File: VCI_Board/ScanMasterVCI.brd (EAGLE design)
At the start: 53 x 39.4 mm, 77 parts, among them IC1 XMEGA16A4A, Q13 MMBT3904, Q14 MMBT3904, Q15 MMBT3904, Q2 NDC7002N, Q3 MMBT3904, Q5 NTZD5110N, Q6 MMBT3904, Q7 ZXMP6A17G, Q8 MMBT4403, Q9 NDC7002N, U1 MAX17502FATB+, U2 SN65HVDA195-Q1, U3 MAX17502EATB+, U4 L78L08ABUTR

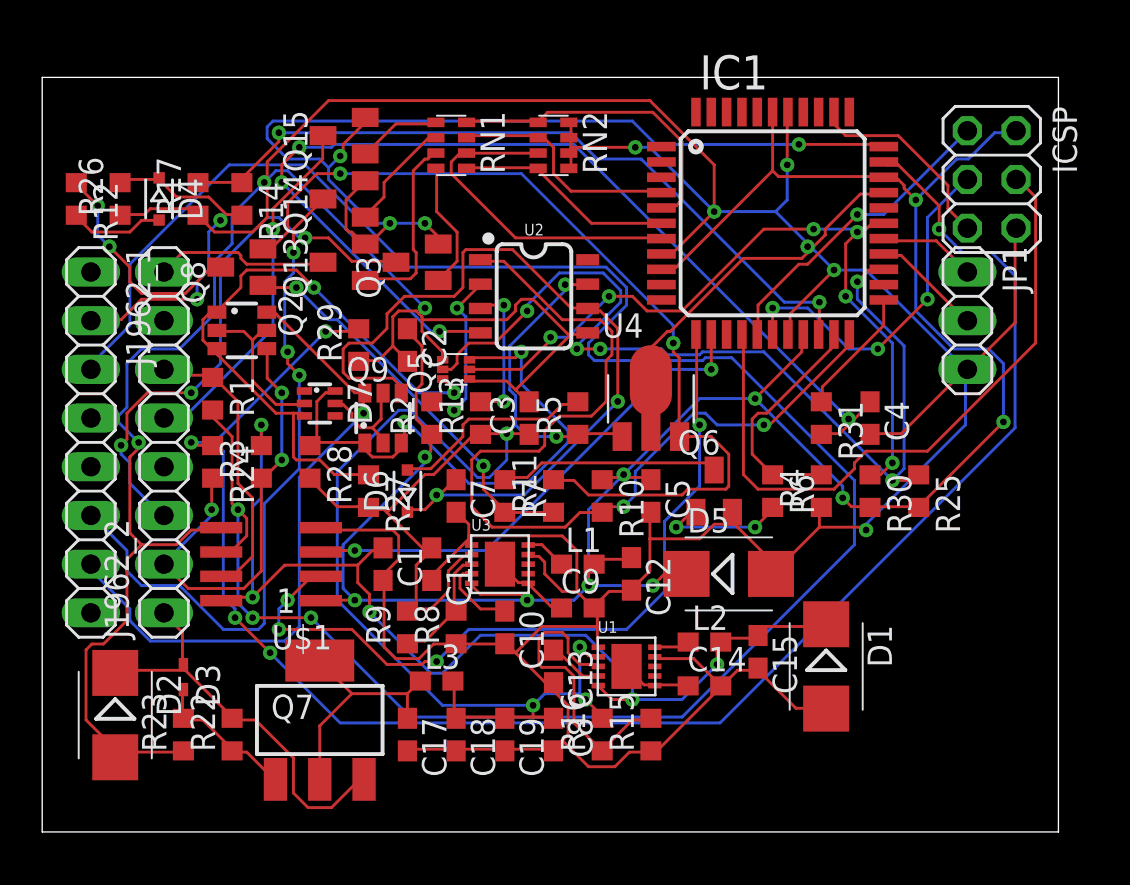
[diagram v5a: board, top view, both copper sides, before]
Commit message: Changed OBD2 connector, refined layout
Decided that it'd be more efficient if I removed all un-used OBD-II pins. Axed about 5 pins and changed the order such that the layout is easier. Managed to get the number of vias down to 68 or so. Separated resistors and capacitors into rows so that I can label them individually.
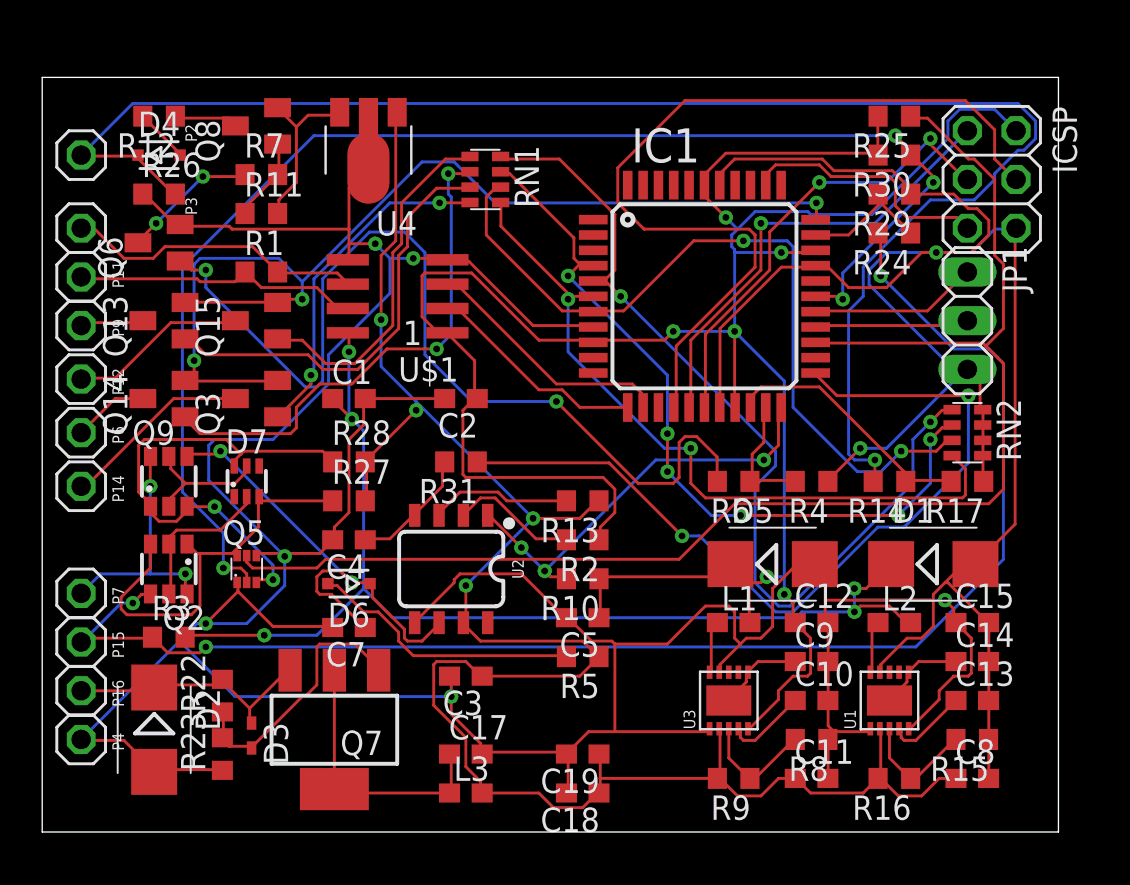
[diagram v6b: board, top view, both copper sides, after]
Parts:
- removed J1962_1, J1962_2: (no value), pinhead:1X08
- added P11, P12, P14, P15, P16, P2, P3, P4, P6, P7, P9: (no value), pinhead:1X01
- moved R17 42.8 mm to (48.3, 20.8), turned to 180 degrees
- moved R24 37.5 mm to (44.5, 33.8), turned to 180 degrees
- moved R14 36.9 mm to (44.2, 20.8), turned to 180 degrees
- moved Q6 31.7 mm to (6.10, 33.3), turned to 90 degrees
- moved R29 29.0 mm to (44.5, 35.8), turned to 180 degrees
- moved C4 27.9 mm to (16.0, 17.8), turned to 180 degrees
- moved RN2 26.3 mm to (48.3, 23.4)
- moved C11 22.7 mm to (40.1, 5.33), turned to 0 degrees
- moved C8 22.0 mm to (48.5, 5.33), turned to 0 degrees
- moved C13 21.9 mm to (48.5, 9.40), turned to 0 degrees
- moved R11 21.2 mm to (11.4, 34.8), turned to 0 degrees
- moved R7 21.0 mm to (11.4, 36.8), turned to 0 degrees
- moved U4 19.6 mm to (17.0, 38.1), turned to 180 degrees
- moved R25 19.6 mm to (44.5, 39.9), turned to 180 degrees
- moved R8 19.4 mm to (40.1, 7.37), turned to 180 degrees
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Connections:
- net GND: now also P4.1; no longer J1962_1.4
- net J1962-11: now also P11.1; no longer J1962_2.6
- net J1962-12: now also P12.1; no longer J1962_2.5
- net J1962-14: now also P14.1; no longer J1962_2.3
- net J1962-15: now also P15.1; no longer J1962_2.2
- net J1962-16: now also P16.1; no longer J1962_2.1
- net J1962-2: now also P2.1; no longer J1962_1.2
- net J1962-3: now also P3.1; no longer J1962_1.3
- net J1962-6: now also P6.1; no longer J1962_1.6
- net J1962-7: now also P7.1; no longer J1962_1.7
- net J1962-9: now also P9.1; no longer J1962_2.8
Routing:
- net J1962-3: track 113.7 -> 15.6 mm, vias 3 -> 0
- net SCI-RX: track 89.3 -> 7.38 mm, vias 5 -> 0
- net J1962-2: track 18.3 -> 82.8 mm, vias 2 -> 1
- net J1962-15: track 24.0 -> 76.0 mm
- net N$10: track 53.9 -> 6.55 mm, vias 4 -> 0
- net N$6: track 6.99 -> 50.1 mm
- net +8V: track 47.5 -> 8.91 mm, vias 2 -> 0
- net ISO-K-TX: track 6.67 -> 44.1 mm, vias 0 -> 2
- net J1962-6: track 36.3 -> 3.95 mm, vias 3 -> 0
- net SCI-B-ENGINE-EN: track 16.5 -> 48.5 mm, vias 0 -> 2
- net SCI-A-TX-EN: track 40.3 -> 71.3 mm, vias 6 -> 4
- net CCD-RX: track 40.6 -> 11.6 mm, vias 4 -> 0
- net SCI-A-ENGINE-EN: track 12.2 -> 40.6 mm, vias 0 -> 6
- net ISO-K-RX: track 49.3 -> 22.4 mm, vias 2 -> 3
- net SCI-A-TRANS-EN: track 11.4 -> 37.9 mm, vias 0 -> 2
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
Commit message: Replaced NDC7002N with NTZD5110N
NDC7002N is out of stock at Digikey, so I am substituting the NTZD5110N. Should be fine, the 5110 just has a lower amp rating than the 7002.
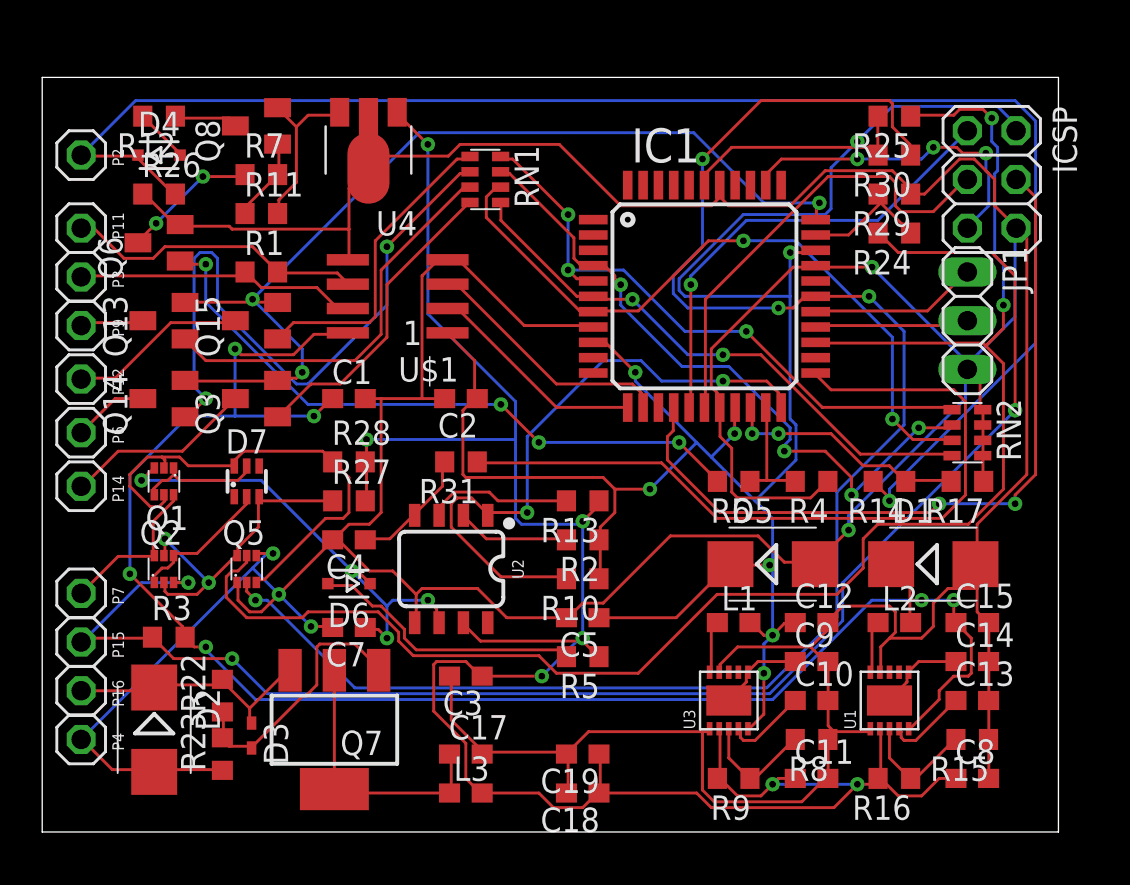
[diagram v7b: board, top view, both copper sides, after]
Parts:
- removed Q9: NDC7002N, customics:SSOT6
- added Q1: NTZD5110N, customics:SOT563
- Q2: value NDC7002N -> NTZD5110N; device customics:SSOT6 -> customics:SOT563
- moved P11 2.54 mm to (2.03, 34.0)
- moved P3 2.54 mm to (2.03, 31.5)
- moved Q2 0.25 mm to (6.35, 16.3), turned to 0 degrees
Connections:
- net ISO-K: now also Q1.3; no longer Q9.4
- net J1962-11: now also R1.2, U$1.6; no longer R1.1, U$1.7
- net J1962-15: now also Q2.3; no longer Q2.4
- net J1962-3: now also R1.1, U$1.7; no longer R1.2, U$1.6
- net J1962-7: now also Q1.6; no longer Q9.6
- net N$1: now also Q2.1, Q2.4; no longer Q2.2, Q2.5
- net N$11: now also Q1.2, Q1.5; no longer Q9.1, Q9.3
- net N$4: now also Q1.1, Q1.4; no longer Q9.2, Q9.5
- net N$5: now also Q2.2, Q2.5; no longer Q2.1, Q2.3
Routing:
- net N$6: track 50.1 -> 34.0 mm, vias 2 -> 4
- net SCI-B-ENGINE-EN: track 48.5 -> 32.4 mm, vias 2 -> 3
- net +5V: track 73.0 -> 88.6 mm
- net SCI-A-TX-EN: track 71.3 -> 86.6 mm
- net +12V: track 101.8 -> 114.4 mm, vias 4 -> 7
- net ISO-K-EN: track 73.5 -> 84.4 mm, vias 0 -> 2
- net ISO-K-RX: track 22.4 -> 33.2 mm, vias 3 -> 2
- net SCI-A-TRANS-EN: track 37.9 -> 29.6 mm
- net N$21: track 26.7 -> 34.4 mm
- net SCI-A-ENGINE-EN: track 40.6 -> 35.1 mm, vias 6 -> 4
- net MOSI: track 45.3 -> 40.2 mm, vias 0 -> 2
- net GND: track 305.0 -> 310.0 mm, vias 7 -> 5
- net J1962-7: track 13.1 -> 8.26 mm, vias 2 -> 0
- net N$5: track 21.7 -> 16.9 mm, vias 0 -> 2
- net SCI-B-TRANS-EN: track 41.0 -> 36.7 mm
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
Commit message: Re-positioned names, removed values
In layout, positioned names so they will be visible during assembly, and deleted values from layout, unneeded. Added another resistor array to save on space, number of vias down to 58.
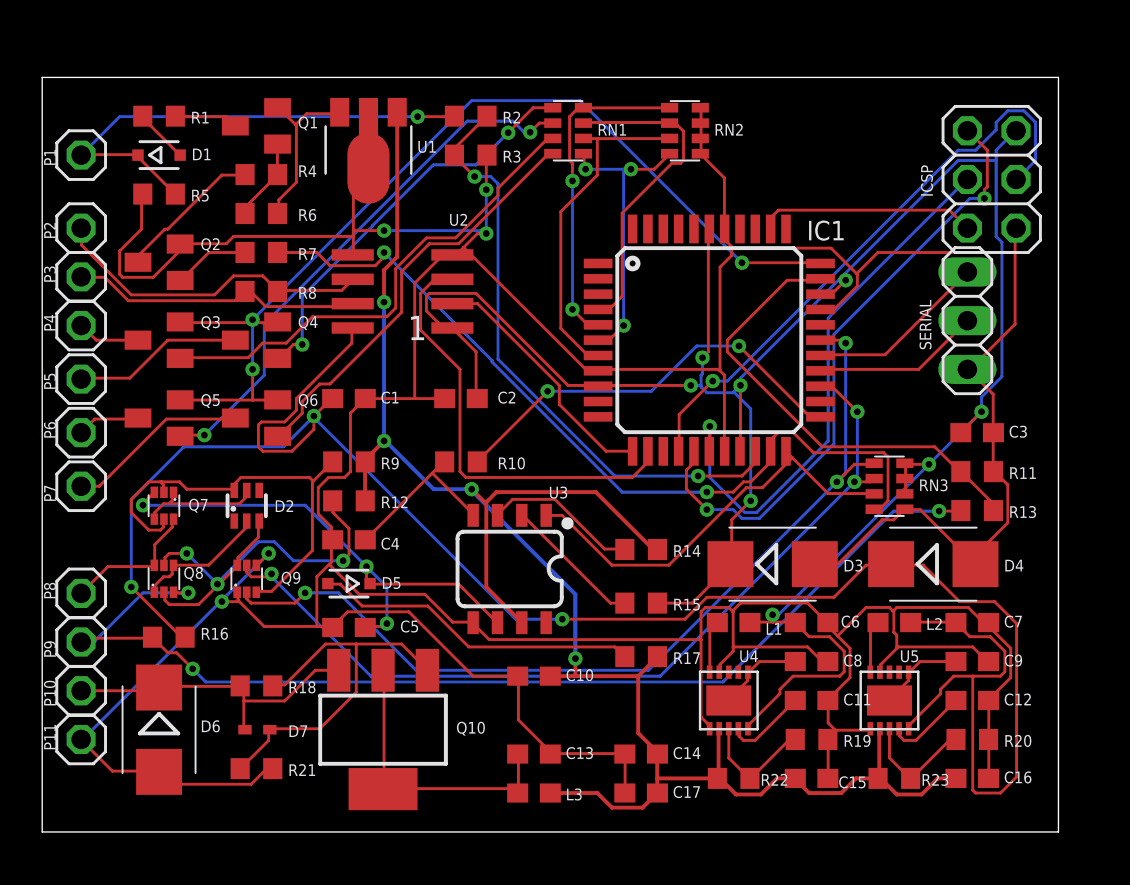
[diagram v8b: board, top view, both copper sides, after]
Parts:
- removed C18: 100uF, adafruit:C0603
- removed C19: 330pF, adafruit:C0603
- removed FRAME1: FRAME-LETTER, SparkFun-Aesthetics:CREATIVE_COMMONS
- removed P14, P15: (no value), pinhead:1X01
- removed Q13, Q14, Q15: MMBT3904, semicon-smd-ipc:SOT23
- removed R24, R31: 1k, adafruit:R0603
- removed R25, R26, R30: 10k, adafruit:R0603
- removed R27, R28: 9.09M, adafruit:R0603
- removed R29: 1910, adafruit:R0603
- removed U$1: ISO1050, customics:SOP08
- added C16: 2.2uF, adafruit:C0603
- added C6: 22uF, adafruit:C0603
- added P1, P8: (no value), pinhead:1X01
- added Q10: ZXMP6A17G, customics:SOT223
- added Q4: MMBT3904, semicon-smd-ipc:SOT23
- added Q9: NTZD5110N, customics:SOT563
- added R18: 200k, adafruit:R0603
- added R19, R20: 866k, adafruit:R0603
- added R21: 20k, adafruit:R0603
- added RN3: 742C083104JP, resistor-net:CTS742C083
- added U5: MAX17502FATB+, customics:TDFN-10
- C10, C13: value 1uF -> 0.1uF
- C11: value 2.2uF -> 1uF
- C12: value 22uF -> 1uF
- C14: value 3300pF -> 330pF
- C15: value 22uF -> 2.2uF
- C17: value 0.1uF -> 100uF
- C5: value 0.1uF -> 220pF
- C7: value 220pF -> 22uF
- C8: value 2.2uF -> 3300pF
- D1: value SMAJ5.0A -> 1N4148WX; device diode:SMB -> diode:SOD323-R
- D2: value 1.5SMC43AT3G -> BZX84C2V4S; device diode:SMB -> customics:SOT363
- D3: value MM5Z10V -> SMLVT3V3; device diode:SOD523 -> diode:SMB
- D4: value 1N4148WX -> SMAJ5.0A; device diode:SOD323-R -> diode:SMB
- D5: value SMLVT3V3 -> 1N4148WX; device diode:SMB -> diode:SOD323-R
- D6: value 1N4148WX -> 1.5SMC43AT3G; device diode:SOD323-R -> diode:SMB
- D7: value BZX84C2V4S -> MM5Z10V; device customics:SOT363 -> diode:SOD523
- Q1: value NTZD5110N -> MMBT4403; device customics:SOT563 -> transistor-pnp:SOT23-BEC
- Q2, Q5: value NTZD5110N -> MMBT3904; device customics:SOT563 -> semicon-smd-ipc:SOT23
- Q7: value ZXMP6A17G -> NTZD5110N; device customics:SOT223 -> customics:SOT563
- Q8: value MMBT4403 -> NTZD5110N; device transistor-pnp:SOT23-BEC -> customics:SOT563
- R1: value 120 -> 47
- R10: value 100K -> 1k
- R11: value 1k -> 1910
- R12: value 47 -> 9.09M
- R13: value 10k -> 1k
- R14: value 7.5k -> 10k
- R15: value 866k -> 100k
- R16: value 3.32M -> 1k
- R17: value 5k -> 1k
- R2: value 100k -> 7.5k
- R22: value 200k -> 3.32M
- R23: value 20k -> 3.32M
- R3: value 1k -> 5k
- R4: value 100k -> 5.1k
- R5: value 1k -> 10k
- R7: value 5.1k -> 1k
- R8: value 866k -> 120
- R9: value 3.32M -> 9.09M
- U1: value MAX17502FATB+ -> L78L08ABUTR; device customics:TDFN-10 -> customics:SOT89
- U2: value SN65HVDA195-Q1 -> ISO1050; device customics:SO08 -> customics:SOP08
- U3: value MAX17502EATB+ -> SN65HVDA195-Q1; device customics:TDFN-10 -> customics:SO08
- U4: value L78L08ABUTR -> MAX17502EATB+; device customics:SOT89 -> customics:TDFN-10
- moved D1 45.7 mm to (6.10, 37.8)
- moved D4 45.7 mm to (46.5, 16.5)
- moved R11 39.7 mm to (48.8, 21.3), turned to 180 degrees
- moved U1 39.5 mm to (17.0, 38.1), turned to 180 degrees
- moved R16 38.6 mm to (6.60, 12.7), turned to 0 degrees
- moved R8 37.0 mm to (11.4, 30.7), turned to 0 degrees
- moved R23 35.1 mm to (44.5, 5.33), turned to 180 degrees
- moved U4 34.3 mm to (35.8, 9.40), turned to 90 degrees
- moved R4 32.9 mm to (11.4, 36.8), turned to 0 degrees
- moved R5 32.7 mm to (6.10, 35.8), turned to 0 degrees
- moved C7 32.5 mm to (48.5, 13.5), turned to 0 degrees
- moved R3 29.7 mm to (22.4, 37.8), turned to 180 degrees
- moved C3 29.5 mm to (48.8, 23.4), turned to 0 degrees
- moved D3 28.6 mm to (38.1, 16.5), turned to 0 degrees
- moved R6 28.3 mm to (11.4, 34.8), turned to 0 degrees
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- renumbered JP1 to SERIAL, P12 to P5, P16 to P10
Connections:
- net +12V: now also C10.1, C14.1, C15.1, C16.1, C17.1, R12.2, R14.1, R17.1, R22.2, R23.2, U1.1, U3.7, U4.2, U5.2; no longer C11.1, C18.1, C19.1, C3.1, C8.1, R13.1, R16.2, R27.2, R28.2, R5.1, U1.2, U2.7, U3.2, U4.1
- net +3V3: now also C3.1, C6.1, D3.C, R15.1, RN3.6, RN3.7, RN3.8, U2.1, U4.5; no longer C12.1, C5.1, D5.C, R10.1, R2.1, R25.2, R30.2, U$1.1, U3.5
- net +5V: now also C7.1, D4.C, R16.2, U2.8, U5.5; no longer C15.1, D1.C, R3.2, U$1.8, U1.5
- net +8V: now also Q1.E, R6.2, U1.3; no longer Q8.E, R11.2, U4.3
- net CCD-RX: now also U2.2; no longer U$1.2
- net CCD-TX: now also U2.3; no longer U$1.3
- net GND: now also C16.2, C6.2, D3.A, D4.A, D6.A, P11.1, Q2.2, Q9.1, Q9.4, R11.1, R19.1, R20.1, R21.1, R3.1, R5.1, RN3.5, U1.2, U1.2@1, U2.4, U3.5, U4.1, U4.9, U5.1, U5.9; no longer C18.2, C19.2, D1.A, D2.A, D5.A, P4.1, Q5.1, Q5.4, Q6.2, R15.1, R17.1, R23.1, R26.1, R29.1, R4.1, R8.1, U$1.4, U$1.5, U1.1, U1.9, U3.1, U3.9, U4.2, U4.2@1
- net ISO-K: now also C5.1, D5.C, Q7.3, U3.6; no longer C7.1, D6.C, Q1.3, U2.6
- net ISO-K-EN: now also Q9.5, RN3.2; no longer Q5.5, R25.1
- net ISO-K-RX: now also RN3.3, U3.1; no longer R10.2, U2.1
- net ISO-K-TX: now also R10.1; no longer R31.1
- net J1850VPW-RX: now also R2.1, R3.2; no longer R14.1, R17.2
- net J1850VPW-TX: now also R7.1, RN3.4; no longer R4.2, R6.1
- net J1962-11: now also P2.1, R8.2, U2.6; no longer P11.1, R1.2, U$1.6
- net J1962-12: now also Q4.3; no longer Q15.3
- net J1962-14: now also P7.1, Q6.3; no longer P14.1, Q3.3
- net J1962-15: now also P9.1, Q8.3, R13.2, R16.1; no longer P15.1, Q2.3, R24.2, R3.1
- net J1962-16: now also D6.C, D7.C, Q10.3, R18.2; no longer D2.C, D3.C, Q7.3, R22.2
- net J1962-2: now also D1.C, P1.1, R2.2, R5.2; no longer D4.C, P2.1, R14.2, R26.2
- net J1962-3: now also R8.1, U2.7; no longer R1.1, U$1.7
- net J1962-6: now also Q5.3; no longer Q14.3
- net J1962-7: now also P8.1, Q7.6, Q8.6; no longer P7.1, Q1.6, Q2.6
- net J1962-9: now also P4.1, Q3.3; no longer P9.1, Q13.3
- net N$1: now also D2.2, Q8.1, Q8.4; no longer D7.2, Q2.1, Q2.4
- net N$10: now also R10.2, U3.4; no longer R31.2, U2.4
- net N$11: now also D2.6, Q7.2, Q7.5, Q9.3, R9.1; no longer D7.6, Q1.2, Q1.5, Q5.3, R28.1
- net N$12: now also U4.10; no longer U3.10
- net N$13: now also Q4.1; no longer Q15.1
- net N$14: now also R14.2, U3.3; no longer R13.2, U2.3
- net N$15: now also C12.1, U5.4; no longer C13.1, U1.4
- net N$16: now also R20.2, R23.1, U5.3; no longer R15.2, R16.1, U1.3
- net N$17: now also C9.1, U5.6, U5.P$11; no longer C14.1, U1.6, U1.P$11
- net N$18: now also C13.1, Q10.2, Q10.4; no longer C17.1, Q7.2, Q7.4
- net N$19: now also U5.10; no longer U1.10
- net N$20: now also D7.A, Q10.1, R18.1, R21.2; no longer D3.A, Q7.1, R22.1, R23.2
- net N$21: now also Q5.1; no longer Q14.1
- net N$22: now also Q3.1; no longer Q13.1
- net N$23: now also Q6.1; no longer Q3.1
- net N$26: now also Q2.3, R4.1; no longer Q6.3, R7.1
- net N$28: now also Q1.B, R4.2, R6.1; no longer Q8.B, R11.1, R7.2
- net N$29: now also Q1.C, R1.1; no longer Q8.C, R12.1
- net N$3: now also C8.1, U4.6, U4.P$11; no longer C9.1, U3.6, U3.P$11
- net N$30: now also D1.A, R1.2; no longer D4.A, R12.2
- net N$31: now also D5.A, R17.2; no longer D6.A, R5.2
- net N$4: now also D2.5, Q7.1, Q7.4; no longer D7.5, Q1.1, Q1.4
- net N$5: now also D2.3, Q8.2, Q8.5, Q9.6, R12.1; no longer D7.3, Q2.2, Q2.5, Q5.6, R27.1
- net N$6: now also Q2.1, R7.2; no longer Q6.1, R6.2
- net N$7: now also R19.2, R22.1, U4.3; no longer R8.2, R9.1, U3.3
- net N$8: now also R15.2, U3.2; no longer R2.2, U2.2
- net N$9: now also C11.1, U4.4; no longer C10.1, U3.4
- net SCI-A-TX-EN: now also Q9.2, RN3.1; no longer Q5.2, R30.1
- net SCI-RX: now also R11.2, R13.1; no longer R24.1, R29.2
- net SCI-TX: now also Q4.2, Q5.2, Q6.2; no longer Q13.2, Q14.2, Q15.2
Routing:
- net J1962-2: track 81.6 -> 26.2 mm
- net ISO-K-EN: track 84.4 -> 46.0 mm, vias 2 -> 3
- net SCI-A-TX-EN: track 86.6 -> 48.3 mm, vias 4 -> 3
- net J1850VPW-TX: track 6.20 -> 43.5 mm, vias 0 -> 2
- net N$6: track 34.0 -> 3.98 mm, vias 4 -> 0
- net J1962-15: track 80.0 -> 58.1 mm
- net GND: track 310.0 -> 288.4 mm
- net +5V: track 88.6 -> 107.6 mm, vias 6 -> 3
- net SCI-B-TRANS-EN: track 36.7 -> 17.7 mm, vias 2 -> 0
- net J1850VPW-RX: track 12.8 -> 31.7 mm
- net ISO-K-TX: track 40.5 -> 21.9 mm, vias 0 -> 2
- net SCI-A-ENGINE-EN: track 35.1 -> 17.2 mm, vias 4 -> 0
- net SCI-RX: track 7.38 -> 24.3 mm
- net +12V: track 114.4 -> 98.8 mm, vias 7 -> 4
- net SCI-B-ENGINE-EN: track 32.4 -> 17.2 mm, vias 3 -> 2
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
